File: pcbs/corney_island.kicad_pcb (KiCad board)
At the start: 2 copper layers, 133.8 x 91.7 mm, 101 parts

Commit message: build: regenerate outlines and PCBs with Ergogen snapshot
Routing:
- net (no net): track 0.00 -> 333.1 mm
- net GND: track 130.3 -> 101.4 mm
- net C5: track 42.7 -> 33.1 mm
- net C3: track 42.7 -> 33.1 mm
- net C1: track 34.5 -> 24.8 mm
- net RST: track 9.64 -> 0.00 mm
- net RAW: track 9.64 -> 0.00 mm
- net C2: track 34.5 -> 24.8 mm
- net P16: track 9.64 -> 0.00 mm
- net C0: track 34.5 -> 24.8 mm
- net P10: track 9.64 -> 0.00 mm
- net C4: track 42.7 -> 33.1 mm
- net VCC: track 111.0 -> 101.4 mm
- net SDA: track 9.63 -> 0.00 mm
- net R3: track 9.63 -> 0.00 mm
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
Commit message: build: regenerate PCBs, images, and gerbers
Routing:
- net (no net): track 333.1 -> 0.00 mm
- net GND: track 101.4 -> 130.3 mm
- net C5: track 33.1 -> 42.7 mm
- net C3: track 33.1 -> 42.7 mm
- net C1: track 24.8 -> 34.5 mm
- net RST: track 0.00 -> 9.64 mm
- net RAW: track 0.00 -> 9.64 mm
- net C2: track 24.8 -> 34.5 mm
- net P10: track 0.00 -> 9.64 mm
- net C0: track 24.8 -> 34.5 mm
- net P16: track 0.00 -> 9.64 mm
- net C4: track 33.1 -> 42.7 mm
- net VCC: track 101.4 -> 111.0 mm
- net SDA: track 0.00 -> 9.63 mm
- net R3: track 0.00 -> 9.63 mm
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
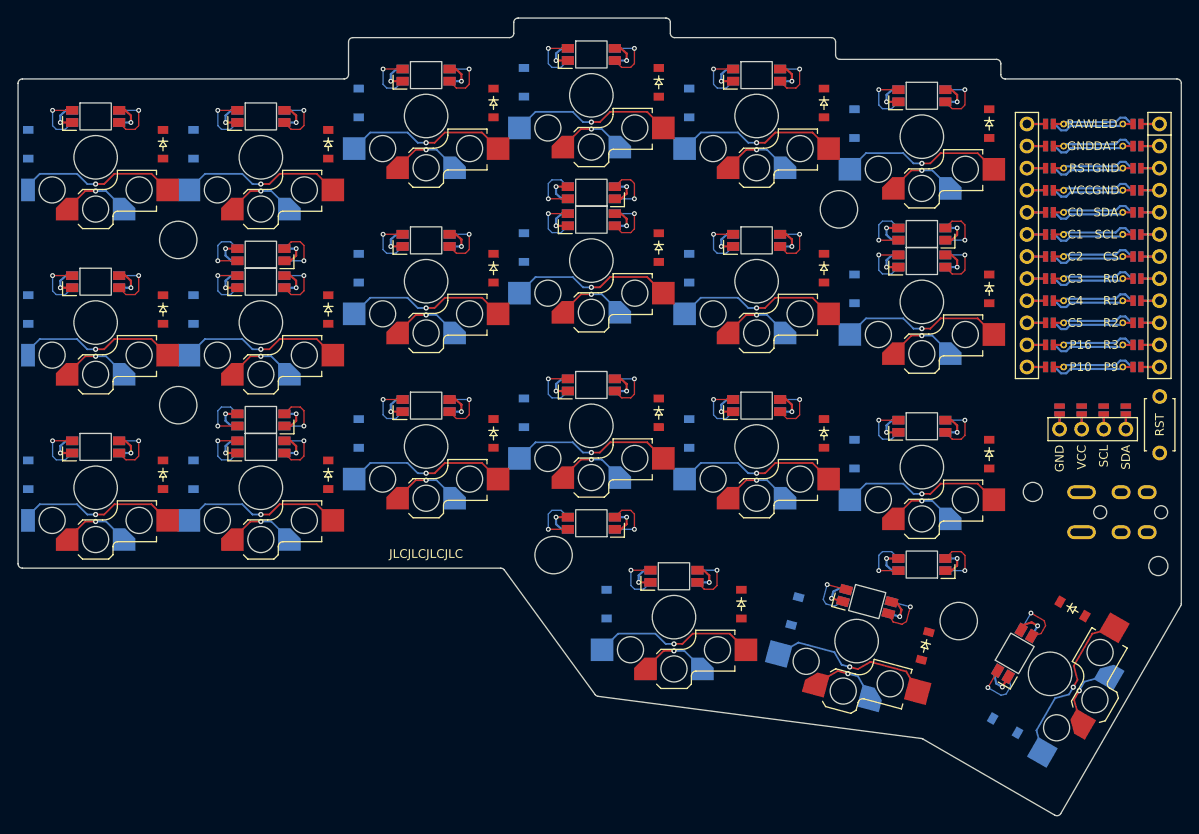
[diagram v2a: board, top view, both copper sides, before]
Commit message: fix(build): restore NPTH normalization and regenerate boards
Normalize source-proven NPTH export obstacles by default, with a native-export opt-out. Pin and verify Freerouting 2.5.1-SNAPSHOT at upstream head 1be66ad and use KiCad 9 for generation, import, and DRC. Make CI run the same build and withhold stale or failing fabrication outputs.

Regenerate the keyboard boards and plates from YAML, including the configured rectangular JST jumpers. Retain routed review boards and unfiltered validation evidence: wireless has one open C4 connection; wired has two open VCC connections. Routing introduces no new KiCad DRC errors. Existing LED clearance and frontplate outline findings remain documented.

Validation: 17 regression tests, actual KiCad 9 export preservation and idempotence checks, post-import DRC, 100 um track-width floor, ShellCheck, shell syntax, workflow YAML validation, and git diff --check.
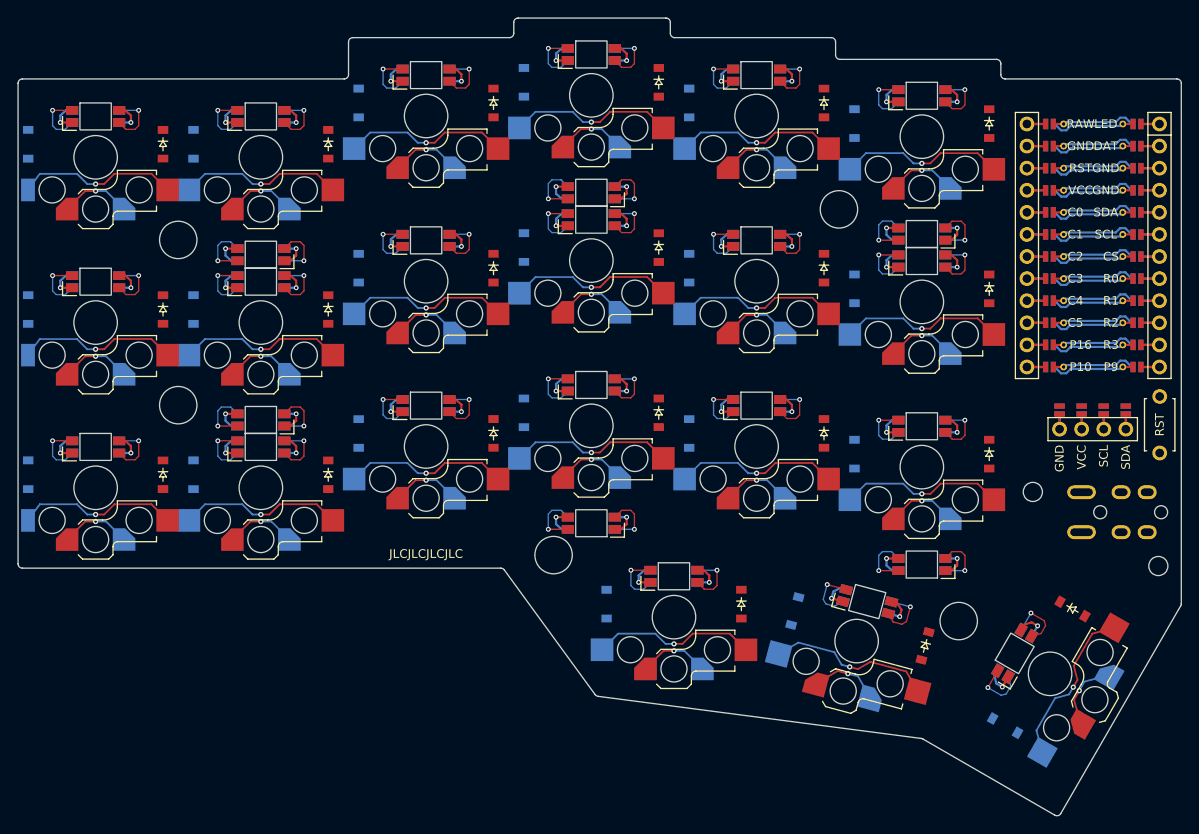
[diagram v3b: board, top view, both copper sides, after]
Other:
- rule pad_to_mask_clearance: 0.05 -> 0

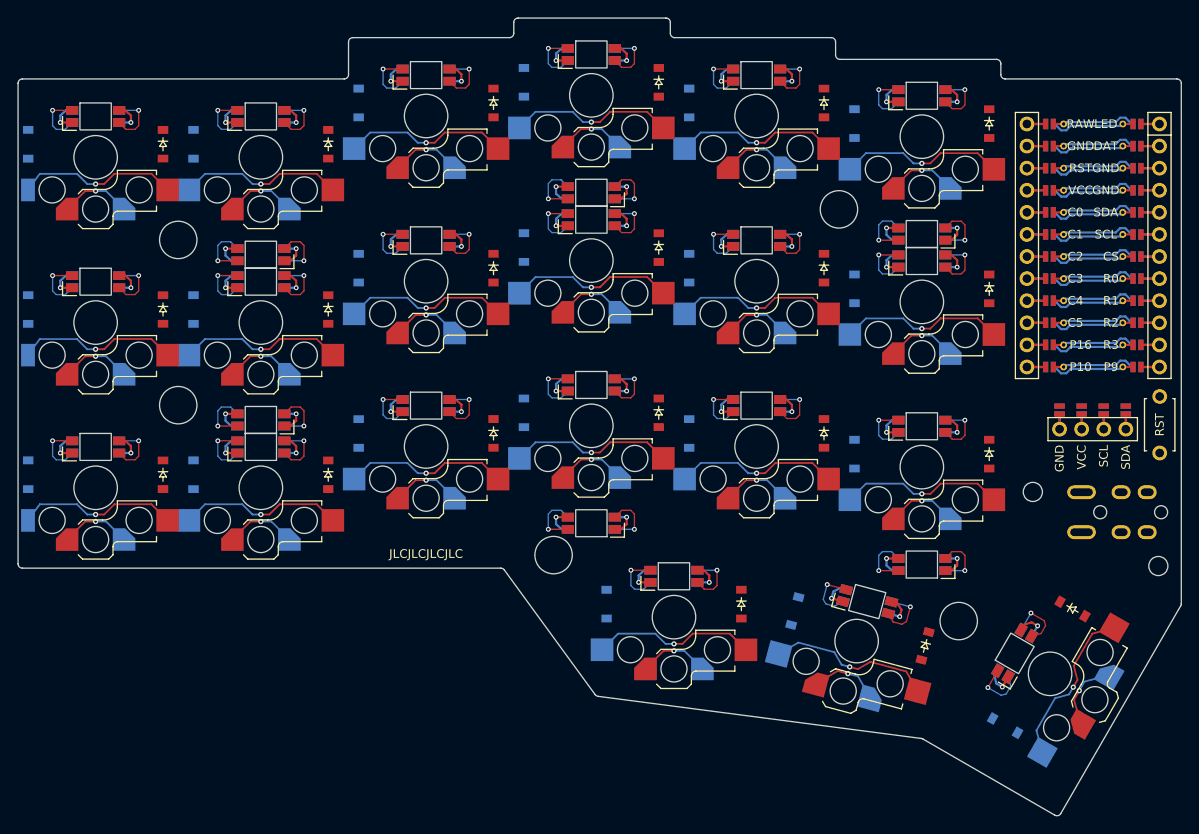
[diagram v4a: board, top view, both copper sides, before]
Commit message: Update LED footprint clearance and refresh generated boards
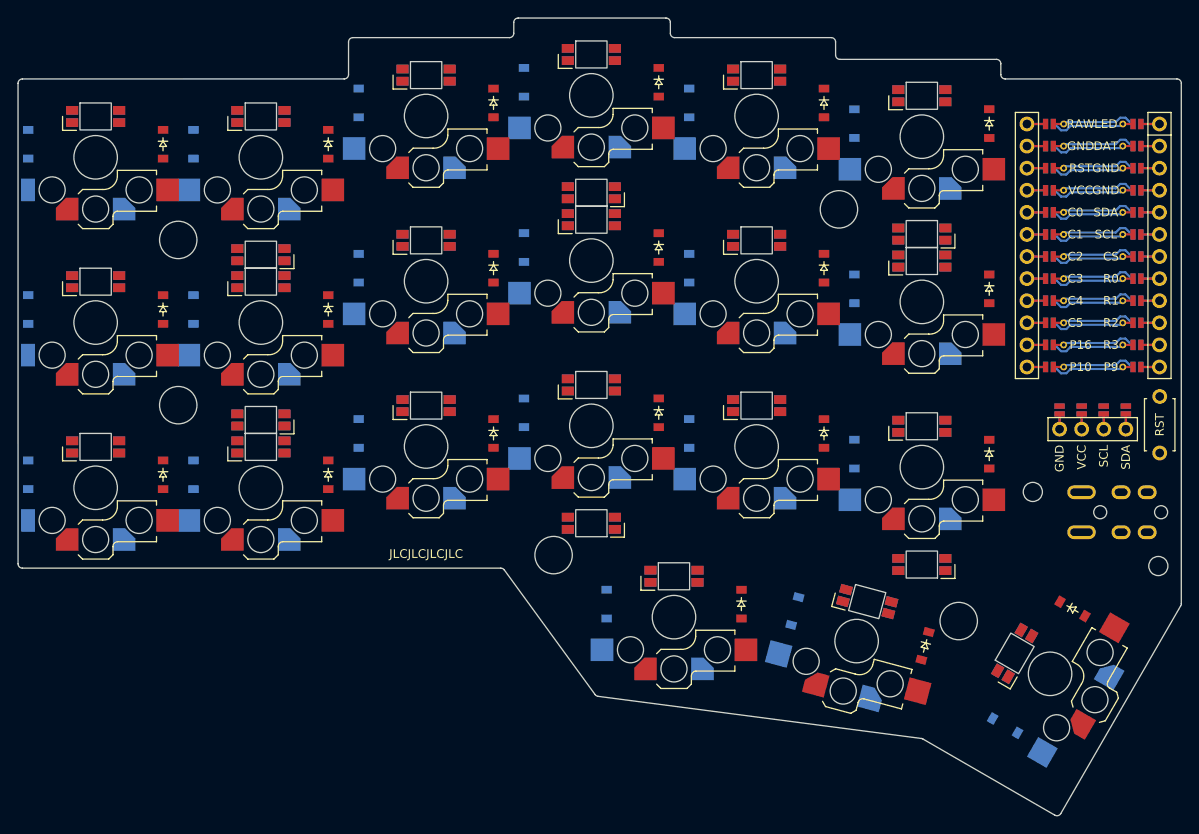
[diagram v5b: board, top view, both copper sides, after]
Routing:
- net GND: track 130.6 -> 29.3 mm, vias 27 -> 0
- net VCC: track 111.1 -> 9.76 mm, vias 27 -> 0
- net C5: track 42.8 -> 9.76 mm, vias 4 -> 0
- net C3: track 42.8 -> 9.76 mm, vias 4 -> 0
- net C4: track 42.8 -> 9.76 mm, vias 4 -> 0
- net C1: track 34.6 -> 9.76 mm, vias 3 -> 0
- net C0: track 34.6 -> 9.76 mm, vias 3 -> 0
- net C2: track 34.6 -> 9.76 mm, vias 3 -> 0
- net mid_home_B: track 19.1 -> 0.00 mm, vias 1 -> 0
- net pinky_top_B: track 19.1 -> 0.00 mm, vias 1 -> 0
- net pinky_home_B: track 19.1 -> 0.00 mm, vias 1 -> 0
- net pinky_bottom_B: track 19.1 -> 0.00 mm, vias 1 -> 0
- net ring_top_B: track 19.1 -> 0.00 mm, vias 1 -> 0
- net ring_home_B: track 19.1 -> 0.00 mm, vias 1 -> 0
- net ring_bottom_B: track 19.1 -> 0.00 mm, vias 1 -> 0
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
